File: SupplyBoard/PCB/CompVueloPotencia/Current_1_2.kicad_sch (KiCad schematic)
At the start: 13 parts, among them U8 INA2180A2

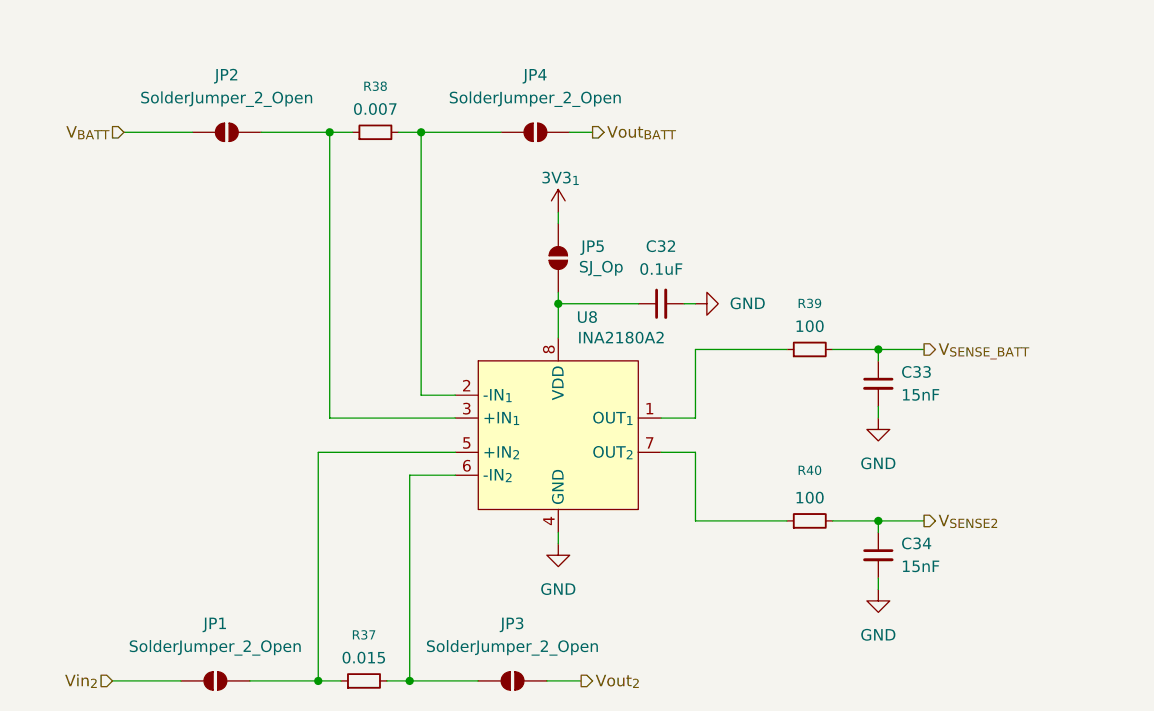
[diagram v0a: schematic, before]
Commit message: SupplyBoard - update layout
schematic completed and PCB layout started; only the routing of the traces remains to be done
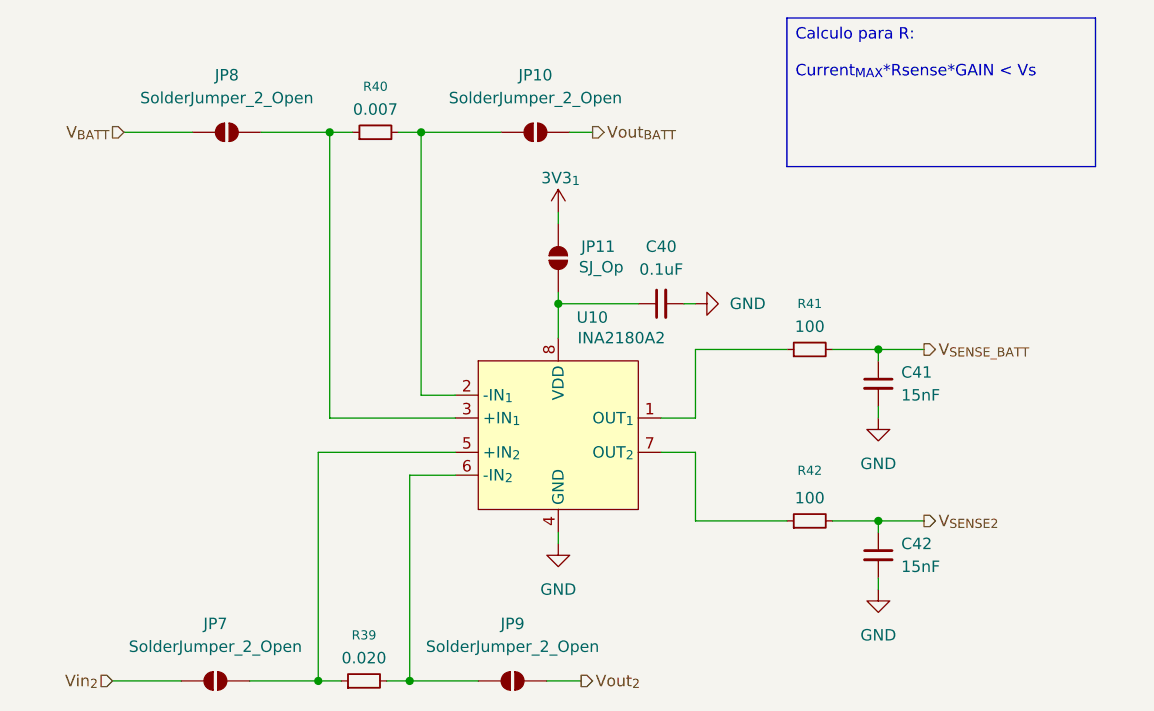
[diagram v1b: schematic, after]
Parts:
- C40: renamed from C32; footprint (none) -> Capacitor_SMD:C_0805_2012Metric_Pad1.18x1.45mm_HandSolder
- C41: renamed from C33; footprint (none) -> Capacitor_SMD:C_0805_2012Metric_Pad1.18x1.45mm_HandSolder
- C42: renamed from C34; footprint (none) -> Capacitor_SMD:C_0805_2012Metric_Pad1.18x1.45mm_HandSolder
- R39: renamed from R37; value 0.015 -> 0.020
- R41: renamed from R39; footprint (none) -> Resistor_SMD:R_0805_2012Metric_Pad1.20x1.40mm_HandSolder
- R42: renamed from R40; footprint (none) -> Resistor_SMD:R_0805_2012Metric_Pad1.20x1.40mm_HandSolder
- U10: renamed from U8; footprint Package_SO:Texas_S-PDSO-G8_3x3mm_P0.65mm -> CompVuelo:Texas_S-PDSO-G8_3x3mm_P0.65mm
- renumbered JP4 to JP10, JP5 to JP11, JP1 to JP7, JP2 to JP8, JP3 to JP9, R38 to R40
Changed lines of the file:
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@@
 	(generator_version "9.0")
 	(paper "A5")
+	(text_box "Calculo para R:\n\nCurrent_{MAX}*Rsense*GAIN < Vs\n"
+		(exclude_from_sim no)
+		(at 130.81 17.78 0)
+		(size 34.29 16.51)
+		(margins 0.9525 0.9525 0.9525 0.9525)
+		(stroke
+			(width 0)
+			(type solid)
+		)
+		(fill
+			(type color)
+			(color 49 49 75 1)
+		)
+		(effects
+			(font
+				(size 1.27 1.27)
+			)
+			(justify left top)
+		)
+	)
 	(junction
 		(at 90.17 30.48)
@@
 		(dnp no)
 		(fields_autoplaced yes)
-		(property "Reference" "R38"
+		(property "Reference" "R40"
 			(at 85.09 25.4 90)
 			(effects
@@
 			(project "SupplyBoardCompVuelo"
 				(path "/2119c5ce-afa8-4b00-8fd4-fc653d4beb45/22ae39d6-ba46-47bf-81b8-3d66f18a6610/b3998068-5005-41ca-89af-5bf3ed5a5126"
-					(reference "R38")
+					(reference "R40")
 					(unit 1)
 				)
@@
 		(dnp no)
 		(fields_autoplaced yes)
-		(property "Reference" "JP1"
+		(property "Reference" "JP7"
 			(at 67.31 85.09 0)
 			(effects
@@
 			(project "SupplyBoardCompVuelo"
 				(path "/2119c5ce-afa8-4b00-8fd4-fc653d4beb45/22ae39d6-ba46-47bf-81b8-3d66f18a6610/b3998068-5005-41ca-89af-5bf3ed5a5126"
-					(reference "JP1")
+					(reference "JP7")
 					(unit 1)
 				)
@@
 		(dnp no)
 		(fields_autoplaced yes)
-		(property "Reference" "JP2"
+		(property "Reference" "JP8"
 			(at 68.58 24.13 0)
 			(effects
@@
 			(project "SupplyBoardCompVuelo"
 				(path "/2119c5ce-afa8-4b00-8fd4-fc653d4beb45/22ae39d6-ba46-47bf-81b8-3d66f18a6610/b3998068-5005-41ca-89af-5bf3ed5a5126"
-					(reference "JP2")
+					(reference "JP8")
 					(unit 1)
 				)
@@
 		(on_board yes)
 		(dnp no)
-		(property "Reference" "#PWR075"
+		(property "Reference" "#PWR092"
 			(at 105.41 43.18 0)
 			(effects
@@
 			(project "SupplyBoardCompVuelo"
 				(path "/2119c5ce-afa8-4b00-8fd4-fc653d4beb45/22ae39d6-ba46-47bf-81b8-3d66f18a6610/b3998068-5005-41ca-89af-5bf3ed5a5126"
-					(reference "#PWR075")
+					(reference "#PWR092")
 					(unit 1)
 				)
@@
 		(on_board yes)
 		(dnp no)
-		(property "Reference" "R40"
+		(property "Reference" "R42"
 			(at 133.35 68.072 90)
 			(effects
@@
 			)
 		)
-		(property "Footprint" ""
+		(property "Footprint" "Resistor_SMD:R_0805_2012Metric_Pad1.20x1.40mm_HandSolder"
 			(at 133.35 73.66 0)
 			(effects
@@
 			(project "SupplyBoardCompVuelo"
 				(path "/2119c5ce-afa8-4b00-8fd4-fc653d4beb45/22ae39d6-ba46-47bf-81b8-3d66f18a6610/b3998068-5005-41ca-89af-5bf3ed5a5126"
-					(reference "R40")
+					(reference "R42")
 					(unit 1)
 				)
@@
 		(dnp no)
 		(fields_autoplaced yes)
-		(property "Reference" "R37"
+		(property "Reference" "R39"
 			(at 83.82 86.36 90)
 			(effects
@@
 			)
 		)
-		(property "Value" "0.015"
+		(property "Value" "0.020"
 			(at 83.82 88.9 90)
 			(effects
@@
 			(project "SupplyBoardCompVuelo"
 				(path "/2119c5ce-afa8-4b00-8fd4-fc653d4beb45/22ae39d6-ba46-47bf-81b8-3d66f18a6610/b3998068-5005-41ca-89af-5bf3ed5a5126"
-					(reference "R37")
+					(reference "R39")
 					(unit 1)
 				)
@@
 		(dnp no)
 		(fields_autoplaced yes)
-		(property "Reference" "C33"
+		(property "Reference" "C41"
 			(at 143.51 57.1562 0)
 			(effects
@@
 			)
 		)
-		(property "Footprint" ""
+		(property "Footprint" "Capacitor_SMD:C_0805_2012Metric_Pad1.18x1.45mm_HandSolder"
 			(at 140.97 58.42 0)
 			(effects
@@
 			(project "SupplyBoardCompVuelo"
 				(path "/2119c5ce-afa8-4b00-8fd4-fc653d4beb45/22ae39d6-ba46-47bf-81b8-3d66f18a6610/b3998068-5005-41ca-89af-5bf3ed5a5126"
-					(reference "C33")
+					(reference "C41")
 					(unit 1)
 				)
@@
 		(on_board yes)
 		(dnp no)
-		(property "Reference" "U8"
+		(property "Reference" "U10"
 			(at 107.442 51.054 0)
 			(effects
@@
 			)
 		)
-		(property "Footprint" "Package_SO:Texas_S-PDSO-G8_3x3mm_P0.65mm"
+		(property "Footprint" "CompVuelo:Texas_S-PDSO-G8_3x3mm_P0.65mm"
 			(at 105.41 63.5 0)
 			(effects
@@
 			(project "SupplyBoardCompVuelo"
 				(path "/2119c5ce-afa8-4b00-8fd4-fc653d4beb45/22ae39d6-ba46-47bf-81b8-3d66f18a6610/b3998068-5005-41ca-89af-5bf3ed5a5126"
-					(reference "U8")
+					(reference "U10")
 					(unit 1)
 				)
@@
 		(dnp no)
 		(fields_autoplaced yes)
-		(property "Reference" "#PWR078"
+		(property "Reference" "#PWR095"
 			(at 140.97 68.58 0)
 			(effects
@@
 			(project "SupplyBoardCompVuelo"
 				(path "/2119c5ce-afa8-4b00-8fd4-fc653d4beb45/22ae39d6-ba46-47bf-81b8-3d66f18a6610/b3998068-5005-41ca-89af-5bf3ed5a5126"
-					(reference "#PWR078")
+					(reference "#PWR095")
 					(unit 1)
 				)
@@
 		(dnp no)
 		(fields_autoplaced yes)
-		(property "Reference" "#PWR076"
+		(property "Reference" "#PWR093"
 			(at 105.41 82.55 0)
 			(effects
@@
 			(project "SupplyBoardCompVuelo"
 				(path "/2119c5ce-afa8-4b00-8fd4-fc653d4beb45/22ae39d6-ba46-47bf-81b8-3d66f18a6610/b3998068-5005-41ca-89af-5bf3ed5a5126"
-					(reference "#PWR076")
+					(reference "#PWR093")
 					(unit 1)
 				)
@@
 		(dnp no)
 		(fields_autoplaced yes)
-		(property "Reference" "JP4"
+		(property "Reference" "JP10"
 			(at 102.87 24.13 0)
 			(effects
@@
 			(project "SupplyBoardCompVuelo"
 				(path "/2119c5ce-afa8-4b00-8fd4-fc653d4beb45/22ae39d6-ba46-47bf-81b8-3d66f18a6610/b3998068-5005-41ca-89af-5bf3ed5a5126"
-					(reference "JP4")
+					(reference "JP10")
 					(unit 1)
 				)
@@
 		(dnp no)
 		(fields_autoplaced yes)
-		(property "Reference" "#PWR079"
+		(property "Reference" "#PWR096"
 			(at 140.97 87.63 0)
 			(effects
@@
 			(project "SupplyBoardCompVuelo"
 				(path "/2119c5ce-afa8-4b00-8fd4-fc653d4beb45/22ae39d6-ba46-47bf-81b8-3d66f18a6610/b3998068-5005-41ca-89af-5bf3ed5a5126"
-					(reference "#PWR079")
+					(reference "#PWR096")
 					(unit 1)
 				)
@@
 		(dnp no)
 		(fields_autoplaced yes)
-		(property "Reference" "#PWR077"
+		(property "Reference" "#PWR094"
 			(at 127 49.53 0)
 			(effects
@@
 			(project "SupplyBoardCompVuelo"
 				(path "/2119c5ce-afa8-4b00-8fd4-fc653d4beb45/22ae39d6-ba46-47bf-81b8-3d66f18a6610/b3998068-5005-41ca-89af-5bf3ed5a5126"
-					(reference "#PWR077")
+					(reference "#PWR094")
 					(unit 1)
 				)
@@
 		(dnp no)
 		(fields_autoplaced yes)
-		(property "Reference" "R39"
+		(property "Reference" "R41"
 			(at 133.35 49.53 90)
 			(effects
@@
 			)
 		)
-		(property "Footprint" ""
+		(property "Footprint" "Resistor_SMD:R_0805_2012Metric_Pad1.20x1.40mm_HandSolder"
 			(at 133.35 54.61 0)
 			(effects
@@
 			(project "SupplyBoardCompVuelo"
 				(path "/2119c5ce-afa8-4b00-8fd4-fc653d4beb45/22ae39d6-ba46-47bf-81b8-3d66f18a6610/b3998068-5005-41ca-89af-5bf3ed5a5126"
-					(reference "R39")
+					(reference "R41")
 					(unit 1)
 				)
@@
 		(dnp no)
 		(fields_autoplaced yes)
-		(property "Reference" "JP3"
+		(property "Reference" "JP9"
 			(at 100.33 85.09 0)
 			(effects
@@
 			(project "SupplyBoardCompVuelo"
 				(path "/2119c5ce-afa8-4b00-8fd4-fc653d4beb45/22ae39d6-ba46-47bf-81b8-3d66f18a6610/b3998068-5005-41ca-89af-5bf3ed5a5126"
-					(reference "JP3")
+					(reference "JP9")
 					(unit 1)
 				)
@@
 		(dnp no)
 		(fields_autoplaced yes)
-		(property "Reference" "C34"
+		(property "Reference" "C42"
 			(at 143.51 76.2062 0)
 			(effects
@@
 			)
 		)
-		(property "Footprint" ""
+		(property "Footprint" "Capacitor_SMD:C_0805_2012Metric_Pad1.18x1.45mm_HandSolder"
 			(at 140.97 77.47 0)
 			(effects
@@
 			(project "SupplyBoardCompVuelo"
 				(path "/2119c5ce-afa8-4b00-8fd4-fc653d4beb45/22ae39d6-ba46-47bf-81b8-3d66f18a6610/b3998068-5005-41ca-89af-5bf3ed5a5126"
-					(reference "C34")
+					(reference "C42")
 					(unit 1)
 				)
@@
 		(dnp no)
 		(fields_autoplaced yes)
-		(property "Reference" "C32"
+		(property "Reference" "C40"
 			(at 116.8463 43.18 90)
 			(effects
@@
 			)
 		)
-		(property "Footprint" ""
+		(property "Footprint" "Capacitor_SMD:C_0805_2012Metric_Pad1.18x1.45mm_HandSolder"
 			(at 116.84 49.53 0)
 			(effects
@@
 			(project "SupplyBoardCompVuelo"
 				(path "/2119c5ce-afa8-4b00-8fd4-fc653d4beb45/22ae39d6-ba46-47bf-81b8-3d66f18a6610/b3998068-5005-41ca-89af-5bf3ed5a5126"
-					(reference "C32")
+					(reference "C40")
 					(unit 1)
 				)
@@
 		(on_board yes)
 		(dnp no)
-		(property "Reference" "JP5"
+		(property "Reference" "JP11"
 			(at 107.95 43.1799 90)
 			(effects
@@
 			(project "SupplyBoardCompVuelo"
 				(path "/2119c5ce-afa8-4b00-8fd4-fc653d4beb45/22ae39d6-ba46-47bf-81b8-3d66f18a6610/b3998068-5005-41ca-89af-5bf3ed5a5126"
-					(reference "JP5")
-					(unit 1)
-				)
+					(reference "JP11")
+					(unit 1)
+				)
